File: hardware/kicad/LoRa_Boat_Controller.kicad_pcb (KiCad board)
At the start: 2 copper layers, 76.2 x 76.2 mm, 45 parts, among them U1 SB007-03Q-TL-E, U3 STM32F4XXR2, U5 TCAN1042H-Q1D, U6 R1240N001x

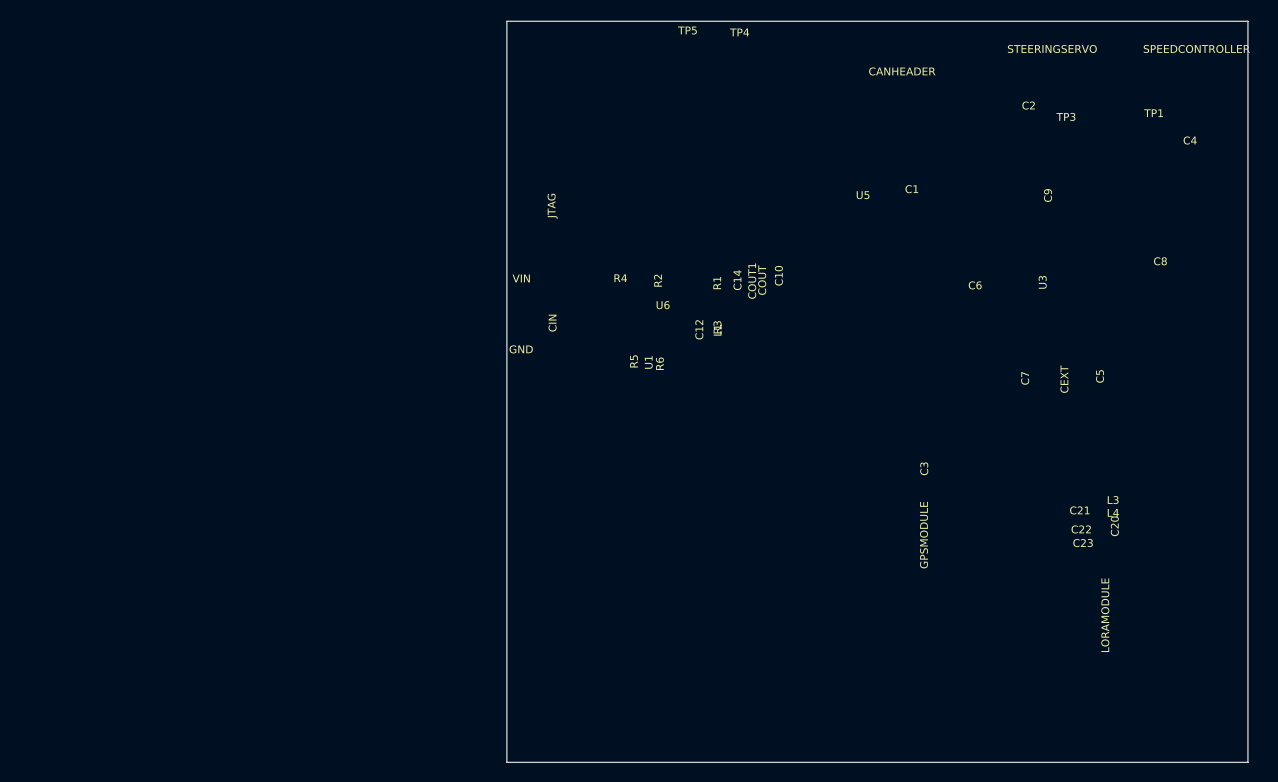
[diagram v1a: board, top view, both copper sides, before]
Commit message: Phase A2: faithful V1 PCB reconstruction from v5 fab films
Reconstruction pipeline in hardware/kicad/tools (provenance, v5_reconstruct, gen_footprints, gen_pcb,
validate_pcb, xor_compare, build_v1). Board is rebuilt from BOATCREW*.art + pstxnet.dat, not the stale DSN v2.
Validated: 172/172 pads at 0.000 mil, DRC 0 errors / 0 unconnected, Gerber XOR F.Cu 0.87 % B.Cu 0.23 %,
drill 53/53. Research notes (datasheets, BOM MPNs, firmware review) added under docs/research.

Co-Authored-By: Claude Fable 5.1 <noreply@anthropic.com>
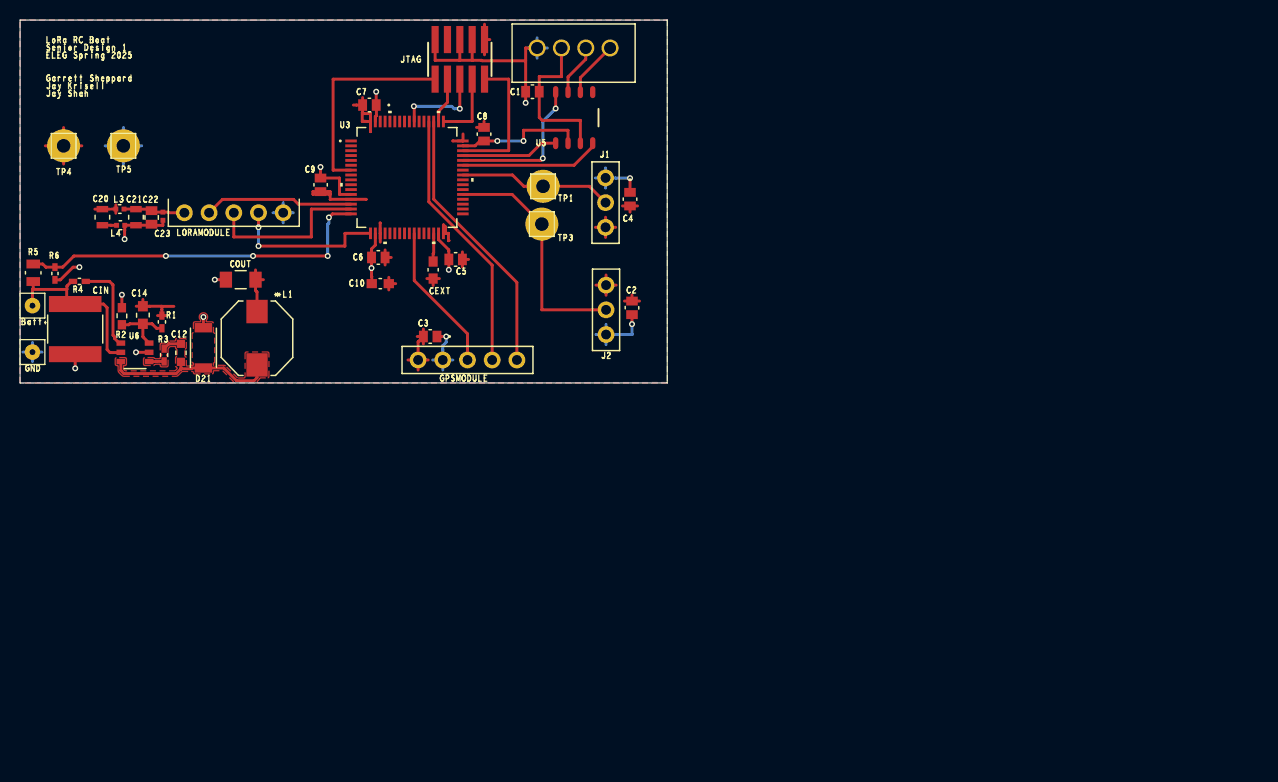
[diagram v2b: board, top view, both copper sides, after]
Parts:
- removed the CANHEADER at (152.5, 69.1)
- removed the CEXT at (171.3, 98.7)
- removed the CIN at (118.6, 92.9)
- removed the COUT at (136.2, 88.5)
- removed COUT1: 10uf, Capacitor_SMD:C_1206_3216Metric
- removed the GND at (113.4, 97.7)
- removed the GPSMODULE at (152.8, 114.7)
- removed the JTAG at (118.5, 80.8)
- removed the LORAMODULE at (171.5, 123.0)
- removed the SPEEDCONTROLLER at (182.8, 66.8)
- removed the STEERINGSERVO at (168.0, 66.8)
- removed U1: SB007-03Q-TL-E, Package_TO_SOT_SMD:SOT-323_SC-70
- removed the VIN at (113.4, 90.4)
- added CANHEADER: CONN_B4B-XH-A, LoRa_Boat_Controller:CONN_B4B-XH-A_JST, F.Cu at (115.0, 64.6)
- added CEXT: 4.7 uF, LoRa_Boat_Controller:CAP_0603_CL10A_1P6XP8_SAM-M, F.Cu at (104.3, 87.5)
- added CIN: 10uF, LoRa_Boat_Controller:CAP_NTS_55_2P8T_NIP, F.Cu at (67.5, 93.5)
- added COUT: 10uf, LoRa_Boat_Controller:G-31_MUR-M, F.Cu at (84.5, 88.5)
- added D21: DIODE_MFLAT, LoRa_Boat_Controller:M-FLAT_TOS-L, F.Cu at (80.7, 95.5)
- added GND: Battery-, LoRa_Boat_Controller:amv_con1, F.Cu at (63.1, 95.9)
- added GPSMODULE: CONN5_1LFBN-RC, LoRa_Boat_Controller:CONN5_1LFBN-RC_SUL, F.Cu at (102.8, 96.7)
- added JTAG: FTSH-105-XX-X-DV, LoRa_Boat_Controller:SAMTEC_FTSH-105-XX-X-DV, F.Cu at (107.1, 65.8)
- added LORAMODULE: CONN5_1LFBN-RC, LoRa_Boat_Controller:CONN5_1LFBN-RC_SUL, F.Cu at (78.7, 81.6)
- added SPEEDCONTROLLER: CONN_PPTC031, LoRa_Boat_Controller:CONN_PPTC031_SUL, F.Cu at (122.0, 83.1)
- added STEERINGSERVO: CONN_PPTC031, LoRa_Boat_Controller:CONN_PPTC031_SUL, F.Cu at (122.1, 89.0)
- added VIN: Battery+, LoRa_Boat_Controller:amv_con1, F.Cu at (63.1, 91.1)
- C1, C2, C3, C4, C5, C6, C7, C8, C9: value 100n -> .1uF; footprint Capacitor_SMD:C_0402_1005Metric -> LoRa_Boat_Controller:CAP_KGM21_KAV-L
- C10: footprint Capacitor_SMD:C_0603_1608Metric -> LoRa_Boat_Controller:CAP_0603_CL10A_1P6XP8_SAM-M
- C12: footprint Capacitor_SMD:C_0603_1608Metric -> LoRa_Boat_Controller:CAP_CL10_SAM-M
- C14: footprint Capacitor_SMD:C_0603_1608Metric -> LoRa_Boat_Controller:CAP_0603G_AVX-M
- C20, C21: footprint Capacitor_SMD:C_0805_2012Metric -> LoRa_Boat_Controller:G-21_MUR-L
- C22: footprint Capacitor_SMD:C_0603_1608Metric -> LoRa_Boat_Controller:CAP_KGM21_KAV-L
- C23: footprint Capacitor_SMD:C_0402_1005Metric -> LoRa_Boat_Controller:CAP_GJM1555C1H220JB01__MUR-L
- L1: value 4.7uH -> 4.7uh; footprint Inductor_SMD:L_0603_1608Metric -> LoRa_Boat_Controller:IND_7045_TDK
- L3, L4: footprint Inductor_SMD:L_0402_1005Metric -> LoRa_Boat_Controller:IND_BLM15_0402_MUR-L
- R1, R4: footprint Resistor_SMD:R_0402_1005Metric -> LoRa_Boat_Controller:RC0402N_PAN-M
- R2: footprint Resistor_SMD:R_0603_1608Metric -> LoRa_Boat_Controller:RC0603N_YAG-M
- R3: footprint Resistor_SMD:R_0402_1005Metric -> LoRa_Boat_Controller:RC0402N_YAG-M
- R5: footprint Resistor_SMD:R_0805_2012Metric -> LoRa_Boat_Controller:RES_R0805_ROM-M
- R6: footprint Resistor_SMD:R_0402_1005Metric -> LoRa_Boat_Controller:RES_1005_SAM-M
- TP1, TP3, TP4, TP5: footprint TestPoint:TestPoint_Pad_D1.0mm -> LoRa_Boat_Controller:amv_test_point
- U3: footprint Package_QFP:LQFP-64_10x10mm_P0.5mm -> LoRa_Boat_Controller:LQFP64-10x10mm
- U5: footprint Package_SO:SOIC-8_3.9x4.9mm_P1.27mm -> LoRa_Boat_Controller:D0008A_L
- U6: footprint Package_TO_SOT_SMD:SOT-23-6 -> LoRa_Boat_Controller:SOT-23-6W_PE-SOT23-6W-0512_NMD
- moved C20 110.8 mm to (70.3, 82.0)
- moved L3 107.0 mm to (72.1, 81.2), turned to 180 degrees
- moved L4 106.8 mm to (72.2, 82.9), turned to 180 degrees
- moved C21 102.3 mm to (73.8, 82.0), turned to 90 degrees
- moved C22 101.5 mm to (75.4, 82.1), turned to 90 degrees
- moved C23 101.1 mm to (76.5, 81.9), turned to 90 degrees
- moved C4 84.6 mm to (98.7, 86.2), turned to 0 degrees
- moved C2 73.1 mm to (92.7, 78.7), turned to -90 degrees
- moved C5 71.0 mm to (104.0, 94.3), turned to 180 degrees
- moved TP4 70.2 mm to (66.3, 74.7)
- moved U3 68.3 mm to (101.6, 78.0), turned to 0 degrees
- moved C3 66.6 mm to (97.8, 70.5), turned to 180 degrees
- moved TP1 63.1 mm to (115.6, 78.9)
- moved C7 62.9 mm to (109.6, 73.5)
- moved R6 60.9 mm to (65.4, 87.8), turned to 90 degrees
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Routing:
- net GND: track 0.00 -> 111.6 mm, vias 0 -> 17
- net +3V3: track 0.00 -> 79.1 mm
- net ADC_VBAT: track 0.00 -> 37.3 mm, vias 0 -> 4
- net GPS_TX_PC10: track 0.00 -> 28.1 mm
- net GPS_RX_PC11: track 0.00 -> 27.2 mm
- net PWM_PC6_SERVOHDR: track 0.00 -> 24.8 mm
- net NRST: track 0.00 -> 21.7 mm
- net VIN_RAW: track 0.00 -> 18.7 mm
- net SW_NODE: track 0.00 -> 18.2 mm
- net LORA_RX_PA1: track 0.00 -> 17.4 mm
- net LORA_RST_PA3: track 0.00 -> 16.3 mm, vias 0 -> 2
- net CAN_VCC: track 0.00 -> 16.1 mm
- net PWM_PA8_ESCHDR: track 0.00 -> 15.8 mm
- net CAN_STB_PA11: track 0.00 -> 15.7 mm, vias 0 -> 2
- net LORA_TX_PA0: track 0.00 -> 15.4 mm
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- added copper zone on F.Cu, net +3V3
- added copper zone on B.Cu, net GND
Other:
- board size 76.2 x 76.2 mm -> 66.5 x 37.3 mm
- rule pad_to_mask_clearance: 0.05 -> 0.254

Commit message: Phase A3: hierarchical V1 schematic generated from pstxnet.dat, ERC clean, netlist == pstxnet
gen_symbols.py (R1240N001x, TCAN1042H-Q1, CMS06 diode, VIN_RAW power symbol per current datasheets),
kicad_sym.py (flattened embedding of KiCad 9 library symbols), gen_sch.py (7 sub-sheets mirroring the OrCAD
blocks, labels/hierarchical pins/power symbols, deterministic symbol paths shared with the PCB via v1_design.py),
check_netlist.py (schematic and board nets == pstxnet.dat, refs and footprint paths match).
ERC 0 violations with --severity-all. Allegro refdes without a trailing digit get a '1' suffix (KiCad annotation
rule); original kept in the Allegro_RefDes property.

Co-Authored-By: Claude Fable 5.1 <noreply@anthropic.com>
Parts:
- renumbered CANHEADER to CANHEADER1, CEXT to CEXT1, CIN to CIN1, COUT to COUT1, GND to GND1, GPSMODULE to GPSMODULE1, JTAG to JTAG1, LORAMODULE to LORAMODULE1, SPEEDCONTROLLER to SPEEDCONTROLLER1, STEERINGSERVO to STEERINGSERVO1, VIN to VIN1

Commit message: Phase A3 close: CANH/CANL net names corrected, BOM with MPNs, DSN-v2 comparison, schematic exports
- gen_pcb.py: N04855 is CANL (U5 pin 6) and N24691 is CANH (U5 pin 7) per pstxnet.dat + TI SLLSES9D; the
  old NETLIST.md had them reversed (Codex review finding R03).
- gen_bom.py: docs/BOM.csv regenerated from the schematic with MPN/manufacturer/description/confidence/price
  columns (research in docs/research/BOM_MPN_RESEARCH.md, prices 2026-09-16).
- a0_xor_dsn.py: DSN v2 copper vs v5 films = 54 % / 63 % mismatch, 0 of 20 vias coincide, 0 of 45 parts unmoved;
  the DSN wiring is unusable for v5 (documented in docs/A0_PROVENANCE.md).
- Schematic PDF and per-sheet SVG exports in docs/img.
Gates: DRC 0 errors / 0 unconnected, ERC 0 violations, netlist check PASS, XOR F.Cu 0.87 % B.Cu 0.23 %.

Co-Authored-By: Claude Fable 5.1 <noreply@anthropic.com>
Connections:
- CANHEADER1 pad 3: CANL -> CANH
- CANHEADER1 pad 4: CANH -> CANL
- U5 pad 6: CANH -> CANL
- U5 pad 7: CANL -> CANH
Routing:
- net CANL: track 5.29 -> 5.80 mm
- net CANH: track 5.80 -> 5.29 mm
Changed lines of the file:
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@@
 			(layers "*.Cu" "*.Mask")
 			(remove_unused_layers no)
-			(net 7 "CANL")
+			(net 6 "CANH")
 			(solder_mask_margin 0)
 			(clearance 0.127)
@@
 			(layers "*.Cu" "*.Mask")
 			(remove_unused_layers no)
-			(net 6 "CANH")
+			(net 7 "CANL")
 			(solder_mask_margin 0)
 			(clearance 0.127)
@@
 			(size 1.249934 0.54991)
 			(layers "F.Cu" "F.Mask" "F.Paste")
-			(net 6 "CANH")
+			(net 7 "CANL")
 			(pinfunction "CANL")
 			(solder_mask_margin 0.0508)
@@
 			(size 1.249934 0.54991)
 			(layers "F.Cu" "F.Mask" "F.Paste")
-			(net 7 "CANL")
+			(net 6 "CANH")
 			(pinfunction "CANH")
 			(solder_mask_margin 0.0508)
@@
 	)
 	(segment
-		(start 119.4564 69.18091)
-		(end 119.4564 67.698312)
+		(start 120.01139 65.7989)
+		(end 120.01139 64.6432)
 		(width 0.3048)
 		(layer "F.Cu")
@@
 	)
 	(segment
-		(start 119.4564 67.698312)
-		(end 122.511512 64.6432)
+		(start 118.1864 69.18091)
+		(end 118.1864 67.62389)
 		(width 0.3048)
 		(layer "F.Cu")
@@
 	)
 	(segment
-		(start 120.01139 65.7989)
-		(end 120.01139 64.6432)
+		(start 118.1864 67.62389)
+		(end 120.01139 65.7989)
 		(width 0.3048)
 		(layer "F.Cu")
-		(net 7)
+		(net 6)
 	)
 	(segment
-		(start 118.1864 69.18091)
-		(end 118.1864 67.62389)
+		(start 119.4564 69.18091)
+		(end 119.4564 67.698312)
 		(width 0.3048)
 		(layer "F.Cu")
@@
 	)
 	(segment
-		(start 118.1864 67.62389)
-		(end 120.01139 65.7989)
+		(start 119.4564 67.698312)
+		(end 122.511512 64.6432)
 		(width 0.3048)
 		(layer "F.Cu")
